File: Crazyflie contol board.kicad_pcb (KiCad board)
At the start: 4 copper layers, 38.1 x 38.1 mm, 97 parts, among them P1 CONN_2, P2 CONN_2, P3 CONN_2, P4 CONN_2, P7 MICRO-B-USB, P9 CONN_1, Q1 PMV31XN, Q2 PMV31XN, Q3 PMV31XN, Q4 PMV31XN, Q5 2N7002, Q6 2N7002, SW1 PUSH ON/OFF, U10 MAX16054, U11 ESP32-WROOM, U12 CP2102N-A01-GQFN24, U3 MPU60X0, U4 HMC5883L, U5 MS5611-01BA03, U6 NUF2221, U7 TPS79301, U8 BQ24075, U9 TPS79301

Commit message: new version
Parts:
- removed C1: 100nF, SM0603_Capa
- removed C6: 4.7uF, SM0603_Capa
- removed R10, R11: NM, SM0603
- removed R7: 100k, SM0603
- removed R8, R9: 10k, SM0603
- added SW2: BOOT, digikey-footprints:Switch_Tactile_SMD_B3U-1000P, F.Cu at (137.2, 116.8)
- R42: footprint SM0402 -> digikey-footprints:0603
- U11: footprint footprints-Lib:ESP32-WROOM-32-Espressif-Symbol-Kicad-62379 -> footprints-Lib:ESP32-WROOM-32
- U12: footprint digikey-footprints:QFN-24-1EP_3x3mm -> digikey-footprints:QFN-24-1EP_4x4mm
- moved R42 4.39 mm to (138.4, 108.0)
- moved U12 3.18 mm to (125.0, 97.3)
- moved U11 0.78 mm to (132.0, 114.1)
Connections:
- U11 pad 21: Net-(U11-Pad21) -> /I2C_SCK_VCCA
- U11 pad 22: Net-(U11-Pad22) -> /I2C_SCL_VCCA
- U12 pad 2: Net-(U12-Pad2) -> AGND
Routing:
- net Net-(U11-Pad39): track 45.2 -> 0.00 mm, vias 27 -> 0
- net /MOTOR1: track 3.95 -> 46.5 mm
- net Net-(U11-Pad35): track 0.00 -> 30.8 mm
- net VCOM: track 43.5 -> 16.3 mm
- net VCCA: track 83.6 -> 110.0 mm, vias 11 -> 13
- net AGND: track 58.3 -> 84.5 mm, vias 12 -> 13
- net Net-(U11-Pad34): track 4.77 -> 29.4 mm
- net /LED_RED: track 25.7 -> 4.79 mm, vias 1 -> 0
- net Net-(U11-Pad21): track 18.6 -> 0.00 mm
- net DGND: track 63.0 -> 44.5 mm, vias 8 -> 6
- net Net-(U11-Pad32): track 17.6 -> 0.00 mm
- net /SNRST: track 17.0 -> 0.00 mm, vias 2 -> 0
- net VCC: track 97.9 -> 81.7 mm, vias 12 -> 9
- net /EXT_I2C_SCL/TX: track 14.8 -> 0.00 mm, vias 1 -> 0
- net Net-(SW2-Pad1): track 0.00 -> 14.6 mm, vias 0 -> 1
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- removed copper zone on Vcc_L3, net +BATT
- removed copper zone on B.Cu, net AGND
- removed copper zone on F.Cu, net AGND
- removed copper zone on B.Cu, net DGND
- removed copper zone on F.Cu, net DGND

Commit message: better version
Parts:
- U11: footprint footprints-Lib:ESP32-WROOM-32 -> footprints-Lib:ESP32-WROOM-32S
- moved U11 0.20 mm to (132.1, 114.3)

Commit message: new version
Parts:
- removed G***: bitcraze, bitcraze
- U12: footprint digikey-footprints:QFN-24-1EP_4x4mm -> footprints-Lib:QFN-24-1EP_4x4mm_new
- moved U11 0.17 mm to (132.1, 114.1)
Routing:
- net /MOTOR1: track 46.5 -> 34.5 mm, vias 1 -> 4
- net Net-(U11-Pad35): track 30.8 -> 32.9 mm
- net VCOM: track 16.3 -> 18.3 mm, vias 8 -> 6
- net AGND: track 84.5 -> 82.7 mm
- net VCCA: track 110.0 -> 111.3 mm
- net /MOTOR3: track 7.06 -> 8.24 mm
- removed copper zone on F.Cu, net VCOM
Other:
- board text removed: "RoHS"
- board text removed: "bitcraze.se"

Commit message: working version
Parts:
- R42: footprint digikey-footprints:0603 -> ESP32-footprints-Lib:0603_new_new
- SW2: footprint digikey-footprints:Switch_Tactile_SMD_B3U-1000P -> ESP32-footprints-Lib:Switch_Tactile_SMD_B3U-1000P_new_new
- U11: footprint footprints-Lib:ESP32-WROOM-32S -> ESP32-footprints-Lib:ESP32-WROOM-32_new
- U12: footprint footprints-Lib:QFN-24-1EP_4x4mm_new -> ESP32-footprints-Lib:QFN-24-1EP_4x4mm_new_new
- moved U12 0.19 mm to (125.2, 97.3)
- moved U11 0.17 mm to (132.1, 114.3)
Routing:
- net Net-(U11-Pad35): track 32.9 -> 33.7 mm
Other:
- board text removed: "20"
- board text removed: "4"
- board text removed: "EXP"
- board text removed: "JTAG"
- board text removed: "M1"
- board text removed: "M2"
- board text removed: "M3"
- board text removed: "M4"

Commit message: improved version
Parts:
- added C1: 4.7uF, ESP32-footprints-Lib:0603_new_new, F.Cu at (126.8, 118.8)
- added C2: 100nF, ESP32-footprints-Lib:0603_new_new, F.Cu at (125.7, 118.8)
- added C3: 100nF, ESP32-footprints-Lib:0603_new_new, B.Cu at (128.4, 95.8)
- added R7: 1k, ESP32-footprints-Lib:0603_new_new, F.Cu at (126.3, 90.7)
- C4: value 100nF -> 4.7uF
- U12: footprint ESP32-footprints-Lib:QFN-24-1EP_4x4mm_new_new -> ESP32-footprints-Lib:QFN-24-1EP_4x4mm_new_new_new
- moved C4 17.6 mm to (129.7, 95.7)
- moved U12 0.08 mm to (125.3, 97.3)
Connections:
- C4 pad 1: VCC -> DGND
- C4 pad 2: DGND -> /POWER/VUSB
- SW2 pad 2: Net-(SW2-Pad2) -> DGND
- U11 pad 1: AGND -> DGND
- U11 pad 15: Net-(U11-Pad15) -> DGND
- U11 pad 2: VCCA -> VCC
- U11 pad 38: Net-(SW2-Pad2) -> DGND
- U11 pad 39: Net-(U11-Pad39) -> DGND
- U12 pad 2: AGND -> DGND
- U12 pad 6: VCCA -> VCC
- U12 pad 7: Net-(U12-Pad7) -> /POWER/VUSB
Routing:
- net VCCA: track 111.3 -> 45.6 mm, vias 13 -> 8
- net AGND: track 82.9 -> 40.3 mm, vias 13 -> 11
- net VCC: track 81.7 -> 101.3 mm, vias 9 -> 8
- net DGND: track 44.5 -> 58.2 mm, vias 6 -> 10
- net /POWER/USBD-: track 18.9 -> 7.24 mm
- net Net-(U1-Pad5): track 10.5 -> 0.00 mm
- net Net-(R7-Pad2): track 0.00 -> 9.63 mm, vias 0 -> 1
- net Net-(U1-Pad6): track 9.49 -> 0.00 mm
- net /POWER/VUSB: track 39.1 -> 45.8 mm
- net Net-(R7-Pad1): track 0.00 -> 4.78 mm, vias 0 -> 1
- net Net-(SW2-Pad2): track 4.16 -> 0.00 mm, vias 1 -> 0
- net /POWER/USBD+: track 21.3 -> 18.1 mm
- net Net-(U1-Pad16): track 13.1 -> 10.4 mm
- net /LED_RED: track 4.79 -> 3.68 mm
- net /I2C_SCL_VCCA: track 33.1 -> 32.5 mm
- added copper zone on F.Cu, net AGND
- added copper zone on F.Cu, net DGND

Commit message: final versrion
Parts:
- added C5: 100nF, ESP32-footprints-Lib:0603_new_new, F.Cu at (123.1, 109.9)
- added Q7: SS8050-G, digikey-footprints:SOT-23-3, F.Cu at (125.9, 113.9)
- added Q8: SS8050-G, digikey-footprints:SOT-23-3, F.Cu at (133.7, 103.7)
- added R10: 10k, ESP32-footprints-Lib:0603_new_new, F.Cu at (133.8, 101.1)
- added R8: 10k, ESP32-footprints-Lib:0603_new_new, F.Cu at (126.9, 103.4)
- added R9: 10k, ESP32-footprints-Lib:0603_new_new, F.Cu at (121.9, 109.9)
- C1: value 4.7uF -> 22uF
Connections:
- U11 pad 16: Net-(U11-Pad16) -> /MOTOR1
- U11 pad 5: /MOTOR1 -> Net-(U11-Pad5)
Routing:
- net Net-(Q7-Pad2): track 0.00 -> 34.2 mm, vias 0 -> 1
- net /MOTOR1: track 34.5 -> 17.4 mm, vias 4 -> 1
- net Net-(Q8-Pad2): track 0.00 -> 17.1 mm, vias 0 -> 1
- net Net-(C5-Pad1): track 0.00 -> 11.6 mm, vias 0 -> 1
- net Net-(Q7-Pad1): track 0.00 -> 9.23 mm
- net Net-(Q8-Pad3): track 14.6 -> 18.3 mm
- net VCC: track 101.3 -> 103.3 mm, vias 8 -> 9
- net Net-(Q8-Pad1): track 0.00 -> 1.66 mm
- net Net-(U11-Pad5): track 0.00 -> 0.80 mm
- added copper zone on B.Cu, net AGND
- added copper zone on B.Cu, net DGND
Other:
- board text removed: "BAT"

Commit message: version 2.0
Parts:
- removed C16, C8: 10nF, SM0603_Capa
- removed C17: 2.2nF, SM0603_Capa
- removed C21: 0.22uF, SM0603_Capa
- removed C22, C7: 4.7uF, SM0603_Capa
- removed C23: 100nF, SM0603_Capa
- removed U3: MPU60X0, MPU60X0
- removed U4: HMC5883L, QFN16_HMC5883L
- added ?: Fiducial_0.75mm_Dia_1.5mm_Outer, Fiducials:Fiducial_0.75mm_Dia_1.5mm_Outer, B.Cu at (156.5, 118.5)
- added ?: Fiducial_0.75mm_Dia_1.5mm_Outer, Fiducials:Fiducial_0.75mm_Dia_1.5mm_Outer, B.Cu at (157.0, 85.0)
- added ?: Fiducial_0.75mm_Dia_1.5mm_Outer, Fiducials:Fiducial_0.75mm_Dia_1.5mm_Outer, B.Cu at (122.5, 85.5)
- added ?: Fiducial_0.75mm_Dia_1.5mm_Outer, Fiducials:Fiducial_0.75mm_Dia_1.5mm_Outer, F.Cu at (122.5, 85.5)
- added ?: Fiducial_0.75mm_Dia_1.5mm_Outer, Fiducials:Fiducial_0.75mm_Dia_1.5mm_Outer, F.Cu at (156.5, 118.5)
- added ?: Fiducial_0.75mm_Dia_1.5mm_Outer, Fiducials:Fiducial_0.75mm_Dia_1.5mm_Outer, F.Cu at (157.0, 85.0)
- added U1: BMX160, digikey-footprints:LGA-14L_2.5x3mm__LSM6DS3, F.Cu at (140.0, 91.0)
- moved C18 1.39 mm to (143.0, 90.5)
- moved C20 1.10 mm to (139.9, 88.0)
- turned C5 to 270 degrees
- turned R8 to 90 degrees
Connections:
- net /POWER/USBD+ renamed /USBD+
- net /POWER/USBD- renamed /USBD-
- C18 pad 1: Net-(C18-Pad1) -> VCCA
- C3 pad 2: /POWER/VUSB -> VCC
- C4 pad 2: /POWER/VUSB -> VCC
- C5 pad 1: Net-(C5-Pad1) -> DGND
- C5 pad 2: DGND -> Net-(C5-Pad2)
- P7 pad 4: Net-(P7-Pad4) -> (no net)
- Q7 pad 3: Net-(C5-Pad1) -> Net-(C5-Pad2)
- R5 pad 1: /LED_RED -> Net-(R5-Pad1)
- R6 pad 1: /LED_GREEN -> Net-(R6-Pad1)
- R8 pad 1: Net-(Q8-Pad2) -> Net-(Q7-Pad1)
- R8 pad 2: Net-(Q7-Pad1) -> Net-(Q8-Pad2)
- R9 pad 2: Net-(C5-Pad1) -> Net-(C5-Pad2)
- U10 pad 5: Net-(U10-Pad5) -> (no net)
- U11 pad 10: Net-(U11-Pad10) -> /EN1
- U11 pad 11: Net-(U11-Pad11) -> (no net)
- U11 pad 12: Net-(U11-Pad12) -> (no net)
- U11 pad 13: Net-(U11-Pad13) -> Net-(R6-Pad1)
- U11 pad 14: Net-(U11-Pad14) -> Net-(R5-Pad1)
- U11 pad 17: Net-(U11-Pad17) -> (no net)
- U11 pad 18: Net-(U11-Pad18) -> (no net)
- U11 pad 19: Net-(U11-Pad19) -> (no net)
- U11 pad 20: Net-(U11-Pad20) -> (no net)
- U11 pad 21: /I2C_SCK_VCCA -> (no net)
- U11 pad 22: /I2C_SCL_VCCA -> (no net)
- U11 pad 24: Net-(U11-Pad24) -> (no net)
- U11 pad 28: Net-(U11-Pad28) -> /CHG
- U11 pad 29: Net-(U11-Pad29) -> (no net)
- U11 pad 3: Net-(C5-Pad1) -> Net-(C5-Pad2)
- U11 pad 30: Net-(U11-Pad30) -> /PGOOD
- U11 pad 31: Net-(U11-Pad31) -> (no net)
- U11 pad 32: Net-(U11-Pad32) -> (no net)
- U11 pad 33: Net-(U11-Pad33) -> /I2C_SCK_VCCA
- U11 pad 36: Net-(U11-Pad36) -> /I2C_SCL_VCCA
- U11 pad 37: Net-(U11-Pad37) -> (no net)
- U11 pad 4: Net-(U11-Pad4) -> (no net)
- U11 pad 5: Net-(U11-Pad5) -> (no net)
- U11 pad 6: Net-(U11-Pad6) -> /EN2
- U11 pad 7: Net-(U11-Pad7) -> /SYSOFF
- U11 pad 8: Net-(U11-Pad8) -> (no net)
- U11 pad 9: Net-(U11-Pad9) -> /INT_GA
- U12 pad 1: Net-(U12-Pad1) -> (no net)
- U12 pad 10: Net-(U12-Pad10) -> (no net)
- U12 pad 11: Net-(U12-Pad11) -> (no net)
- U12 pad 12: Net-(U12-Pad12) -> (no net)
- U12 pad 13: Net-(U12-Pad13) -> (no net)
- U12 pad 14: Net-(U12-Pad14) -> (no net)
- U12 pad 15: Net-(U12-Pad15) -> (no net)
- U12 pad 16: Net-(U12-Pad16) -> (no net)
- U12 pad 17: Net-(U12-Pad17) -> (no net)
- U12 pad 18: Net-(U12-Pad18) -> (no net)
- U12 pad 22: Net-(U12-Pad22) -> (no net)
- U12 pad 24: Net-(U12-Pad24) -> (no net)
- U12 pad 7: /POWER/VUSB -> VCC
- U12 pad 8: Net-(U12-Pad8) -> (no net)
- U5 pad 6: Net-(U5-Pad6) -> (no net)
- U6 pad 5: /POWER/USB_CON -> VCC
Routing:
- net Net-(R6-Pad1): track 0.00 -> 42.5 mm, vias 0 -> 4
- net /EN2: track 8.98 -> 39.3 mm, vias 1 -> 3
- net /EN1: track 14.6 -> 43.2 mm, vias 1 -> 2
- net /SYSOFF: track 11.8 -> 40.4 mm, vias 1 -> 2
- net /LED_GREEN: track 27.0 -> 0.00 mm, vias 3 -> 0
- net AGND: track 40.3 -> 15.5 mm, vias 11 -> 6
- net /POWER/USB_CON: track 22.4 -> 0.00 mm, vias 4 -> 0
- net Net-(R5-Pad1): track 0.00 -> 19.1 mm, vias 0 -> 2
- net /PGOOD: track 36.3 -> 51.3 mm, vias 2 -> 3
- net Net-(C5-Pad2): track 0.00 -> 11.6 mm, vias 0 -> 1
- net Net-(C5-Pad1): track 11.6 -> 0.00 mm, vias 1 -> 0
- net /I2C_SCL_VCCA: track 32.5 -> 43.9 mm
- net Net-(U1-Pad16): track 10.4 -> 0.00 mm, vias 1 -> 0
- net Net-(U3-Pad7): track 9.23 -> 0.00 mm, vias 2 -> 0
- net Net-(U3-Pad6): track 8.73 -> 0.00 mm, vias 2 -> 0
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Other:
- board size 38.1 x 38.1 mm -> 40.1 x 38.1 mm
- board text added: "4"
- board text added: "BOOT"
- board text added: "Rev.2.0"
- board text removed: "19"
- board text removed: "R24"
- board text removed: "R25"
- board text removed: "R26"

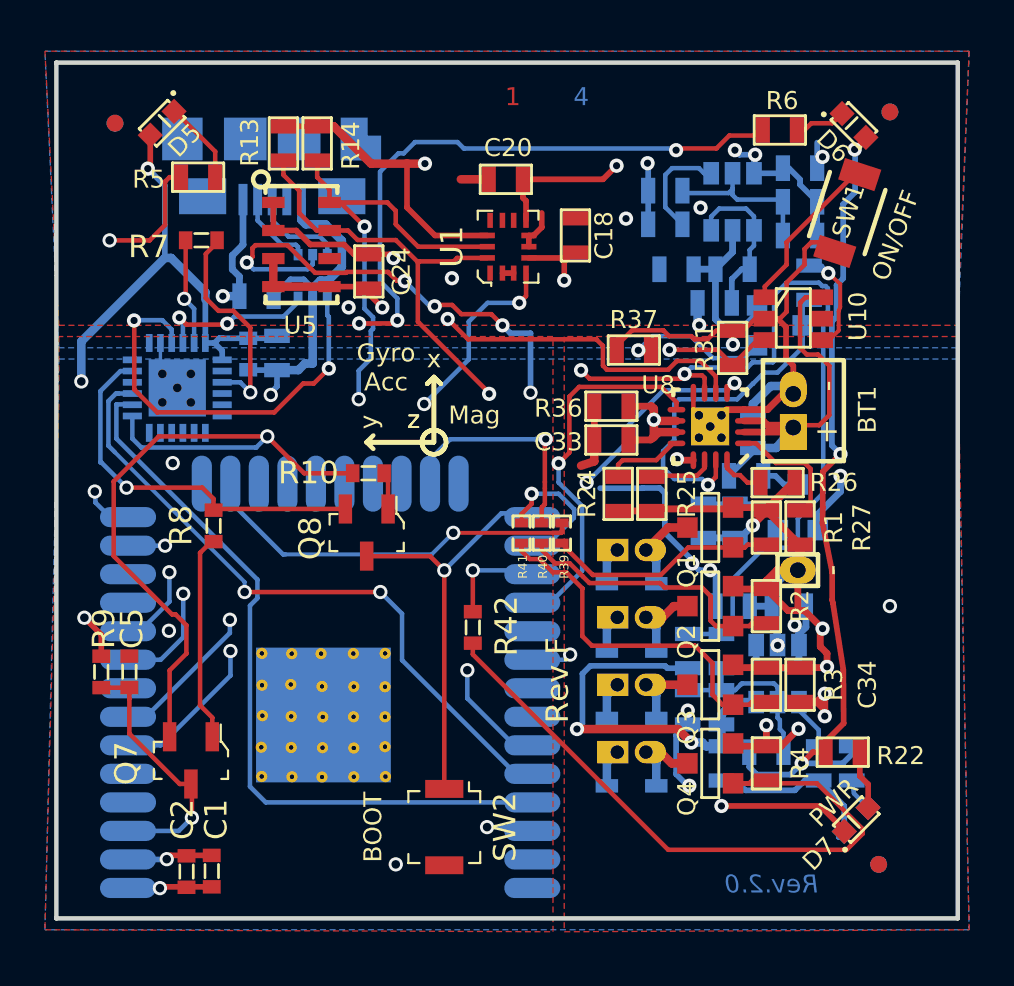
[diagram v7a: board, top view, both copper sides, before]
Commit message: checked: esp32 pins (issue #2)
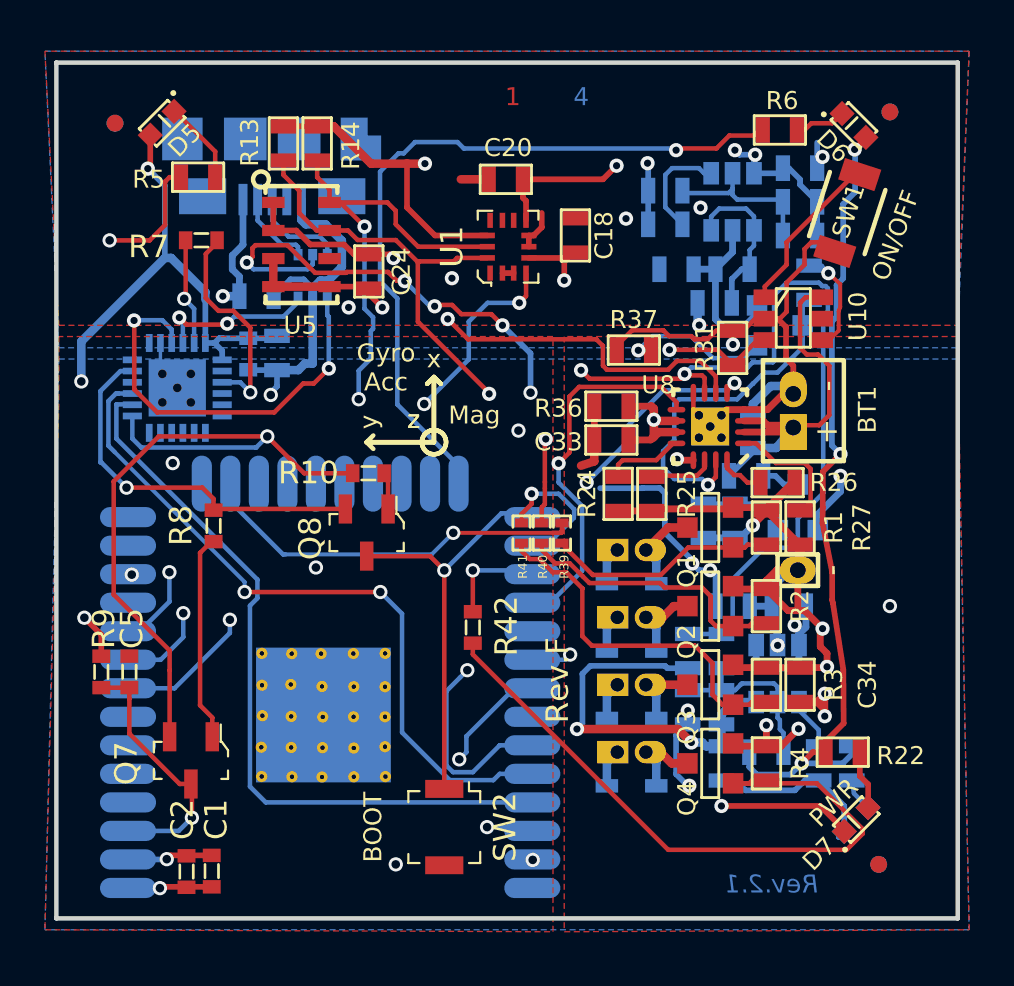
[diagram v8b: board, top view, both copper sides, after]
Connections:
- R5 pad 1: Net-(R5-Pad1) -> /Red
- U11 pad 12: (no net) -> /EN2
- U11 pad 13: Net-(R6-Pad1) -> (no net)
- U11 pad 14: Net-(R5-Pad1) -> (no net)
- U11 pad 23: /MOTOR2 -> (no net)
- U11 pad 24: (no net) -> Net-(R6-Pad1)
- U11 pad 31: (no net) -> /Red
- U11 pad 37: (no net) -> /MOTOR2
- U11 pad 6: /EN2 -> (no net)
- U11 pad 7: /SYSOFF -> (no net)
- U11 pad 8: (no net) -> /SYSOFF
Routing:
- net /Red: track 0.00 -> 46.9 mm, vias 0 -> 2
- net Net-(R5-Pad1): track 19.1 -> 0.00 mm, vias 2 -> 0
- net /MOTOR2: track 10.3 -> 22.8 mm, vias 1 -> 2
- net Net-(R6-Pad1): track 42.5 -> 33.4 mm, vias 4 -> 1
- net /I2C_SCK_VCCA: track 36.8 -> 41.7 mm
- net Net-(U11-Pad34): track 29.4 -> 32.5 mm
- net /EN2: track 39.3 -> 38.0 mm
- net Net-(Q7-Pad2): track 32.6 -> 31.9 mm
- net /SYSOFF: track 40.4 -> 39.8 mm
- net VCC: track 105.9 -> 105.4 mm
- net DGND: vias 10 -> 11
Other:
- board text added: "Rev.2.1"
- board text removed: "Rev.2.0"
